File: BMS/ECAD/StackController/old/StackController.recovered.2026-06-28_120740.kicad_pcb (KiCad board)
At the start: 2 copper layers, 85.8 x 62 mm, 209 parts, among them Q1 BC846, Q2 BC846, U1 TLE9012, U2 TMUX1309A, U3 TMUX1309A

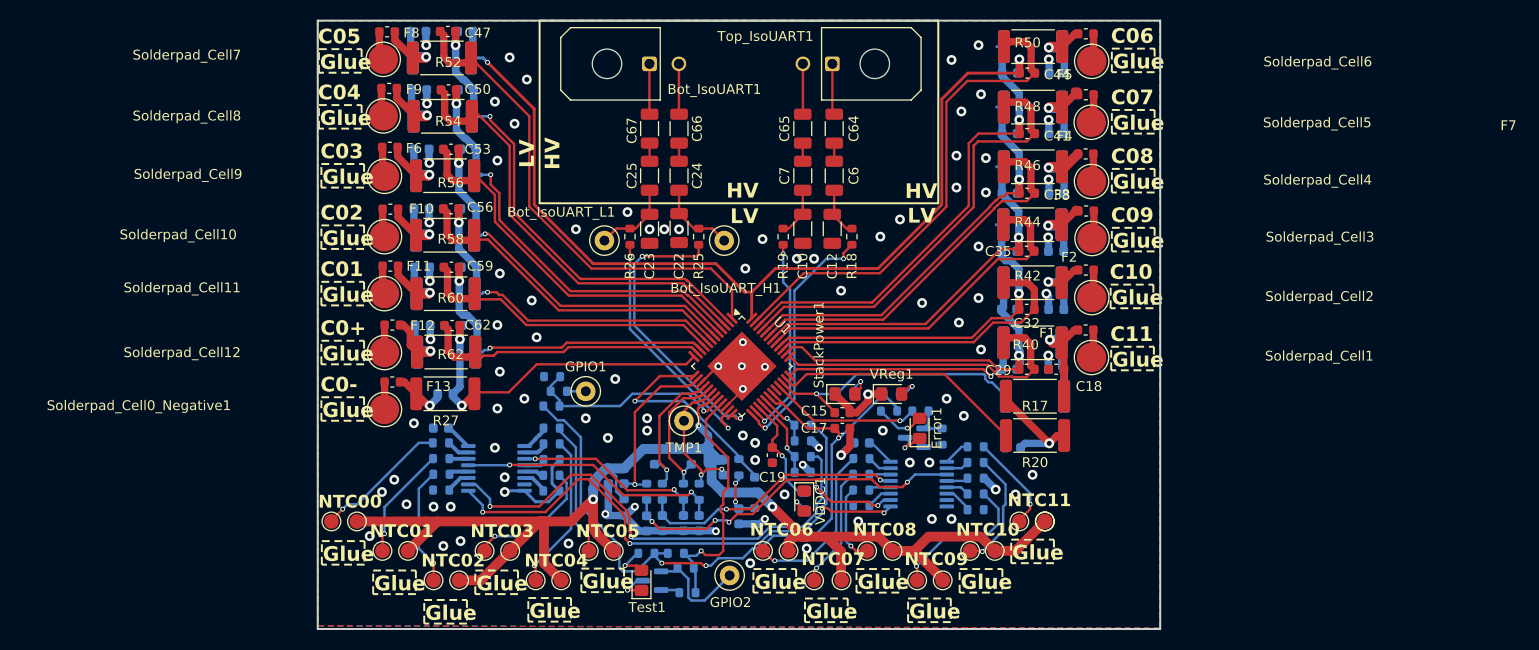
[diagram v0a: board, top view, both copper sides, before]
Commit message: stack controller design close to finished
look into mounting option
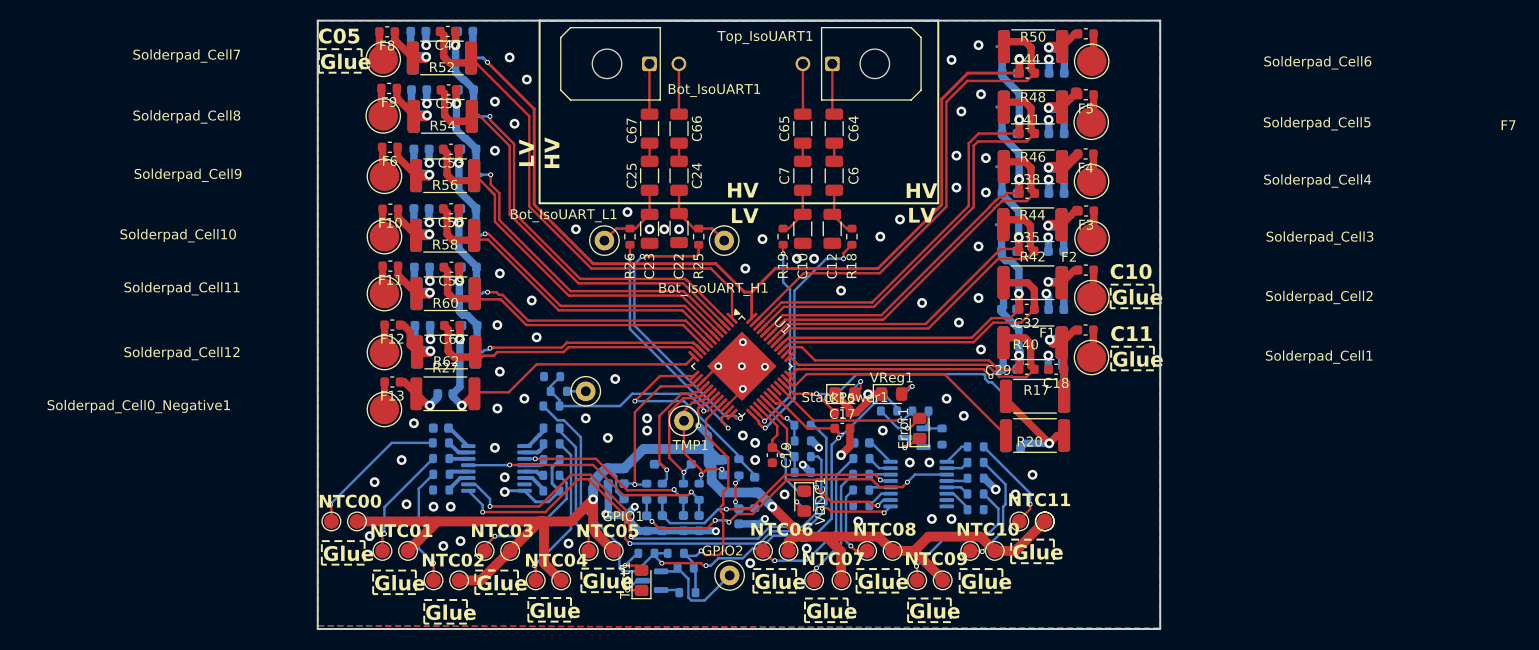
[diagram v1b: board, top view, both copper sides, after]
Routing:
- net NTC02: track 13.7 -> 14.8 mm
- net /Balancing_8/G: track 39.2 -> 40.2 mm
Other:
- board text removed: "C0+"
- board text removed: "C0-"
- board text removed: "C01"
- board text removed: "C02"
- board text removed: "C03"
- board text removed: "C04"
- board text removed: "C06"
- board text removed: "C07"
- board text removed: "C08"
- board text removed: "C09"
